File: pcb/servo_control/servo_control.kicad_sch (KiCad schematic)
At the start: 39 parts, among them J1 USB_B_Micro, J10 Conn_01x03_Female, J11 Conn_01x03_Female, J12 Conn_01x03_Female, J13 Conn_01x03_Female, J14 Conn_01x03_Female, J15 Conn_01x03_Female, J16 Conn_01x03_Female, J17 Conn_01x03_Female, J18 Conn_01x03_Female, J19 Conn_01x03_Female, J2 Conn_02x03_Counter_Clockwise, J20 Conn_01x03_Female, J3 Conn_01x03_Female, J4 Conn_01x03_Female, J5 Conn_01x03_Female, J6 Conn_01x03_Female, J7 Conn_01x03_Female, J8 Conn_01x03_Female, J9 Conn_01x03_Female, U1 ATmega2560-16A, U2 LM317_SOT-223, U3 ESP32-WROOM-32

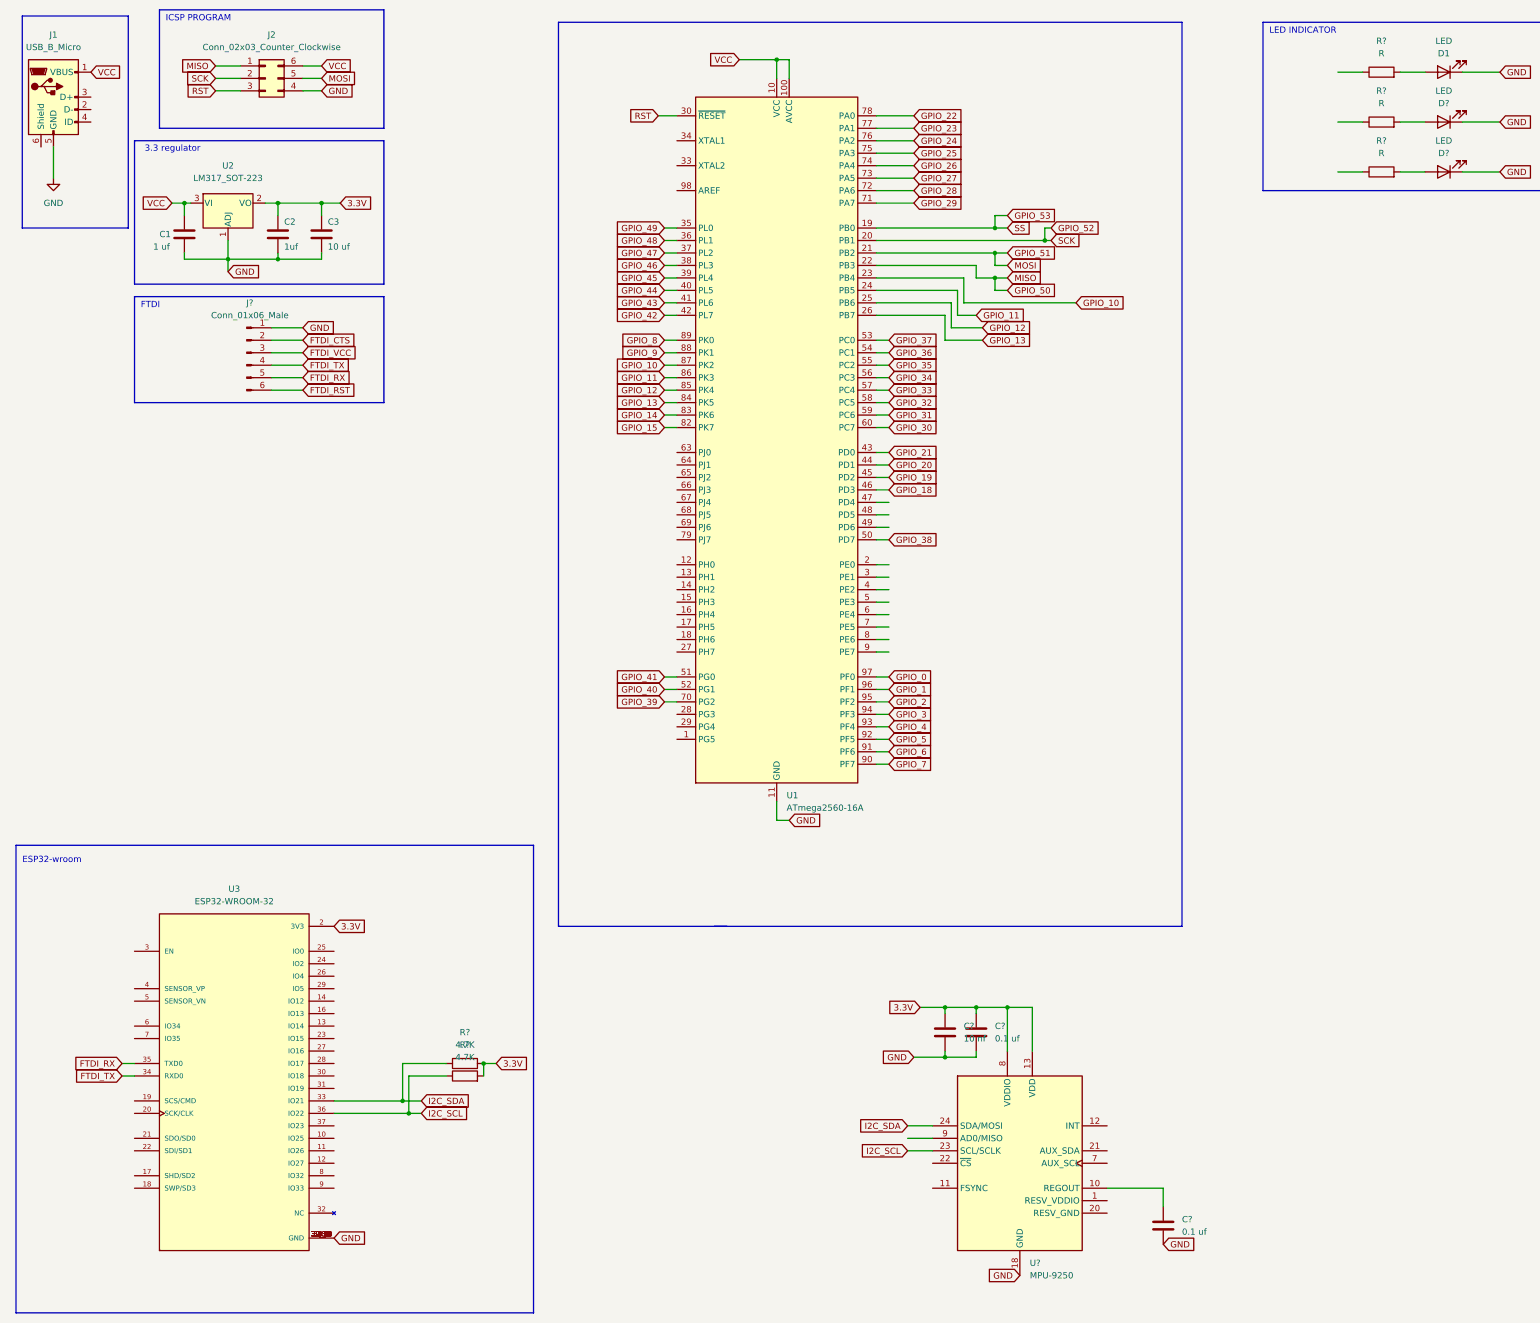
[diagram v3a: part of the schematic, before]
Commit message: add i2c
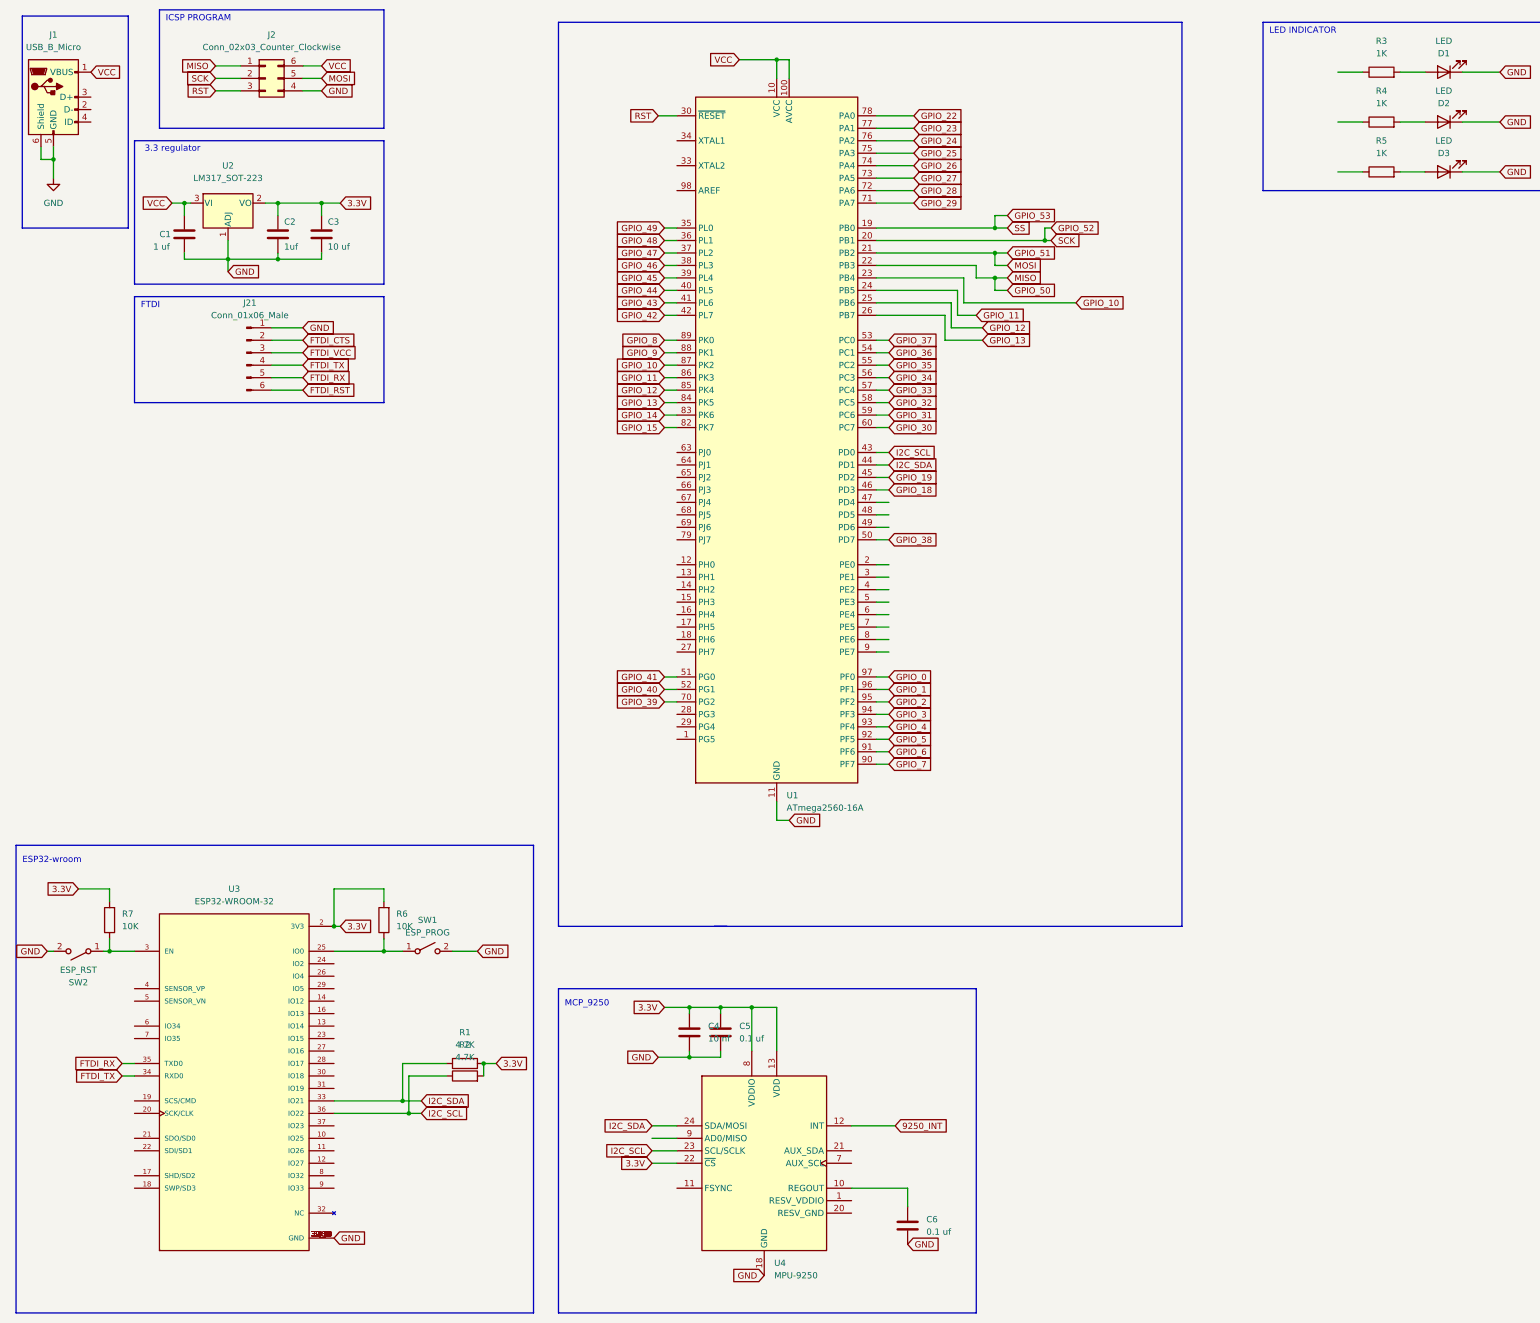
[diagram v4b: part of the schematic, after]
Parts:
- added R6, R7: 10K, Resistor_SMD:R_0603_1608Metric, symbol Device:R
- added SW1: ESP_PROG, Button_Switch_SMD:SW_DIP_SPSTx01_Slide_6.7x4.1mm_W6.73mm_P2.54mm_LowProfile_JPin, symbol Switch:SW_SPST
- added SW2: ESP_RST, Button_Switch_SMD:SW_DIP_SPSTx01_Slide_6.7x4.1mm_W6.73mm_P2.54mm_LowProfile_JPin, symbol Switch:SW_SPST
- C4, C5, C6: renamed from C?; footprint (none) -> Capacitor_SMD:C_0603_1608Metric
- J21: renamed from J?; footprint (none) -> Connector_PinHeader_2.54mm:PinHeader_1x06_P2.54mm_Vertical
- R1, R2: renamed from R?; footprint (none) -> Resistor_SMD:R_0603_1608Metric
- R3, R4, R5: renamed from R?; value R -> 1K; footprint (none) -> Resistor_SMD:R_0603_1608Metric
- gave numbers to parts that had none: 3
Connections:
- net GPIO_20 is gone; now on net I2C_SDA: U1.44 (PD1)
- net 3.3V: now also U4.22 (~{CS}), R6.2, R7.2
- net GND: now also J1.6 (Shield), SW1.2 (B), SW2.2 (B)
- net GPIO_21: no longer U1.43 (PD0)
- net I2C_SCL: now also U1.43 (PD0)
- net 9250_INT: now reaches U4.12 (INT)
- net at U3.25 (IO0): now also R6.1, SW1.1 (A)
- net at U3.3 (EN): now also R7.1, SW2.1 (A)
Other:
- note added: "MCP_9250"
- moved on the sheet: C4, C5, C6, U4

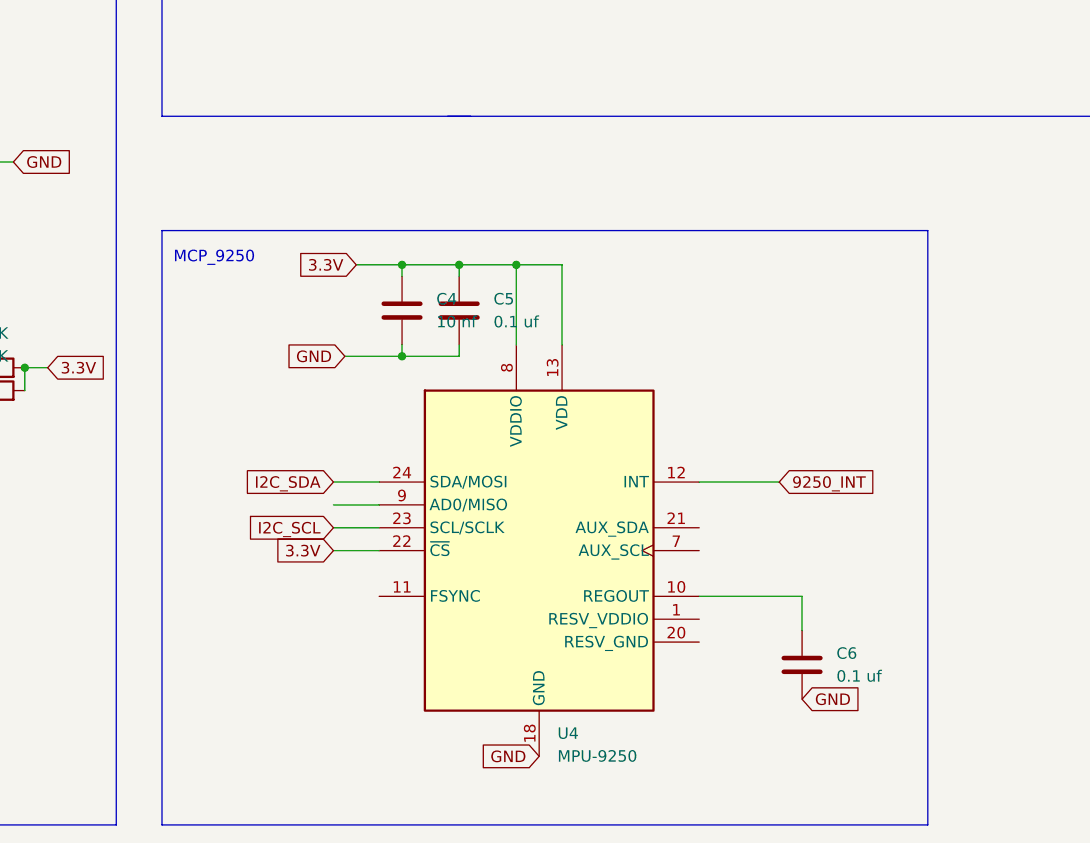
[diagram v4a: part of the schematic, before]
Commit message: add track vcc servo
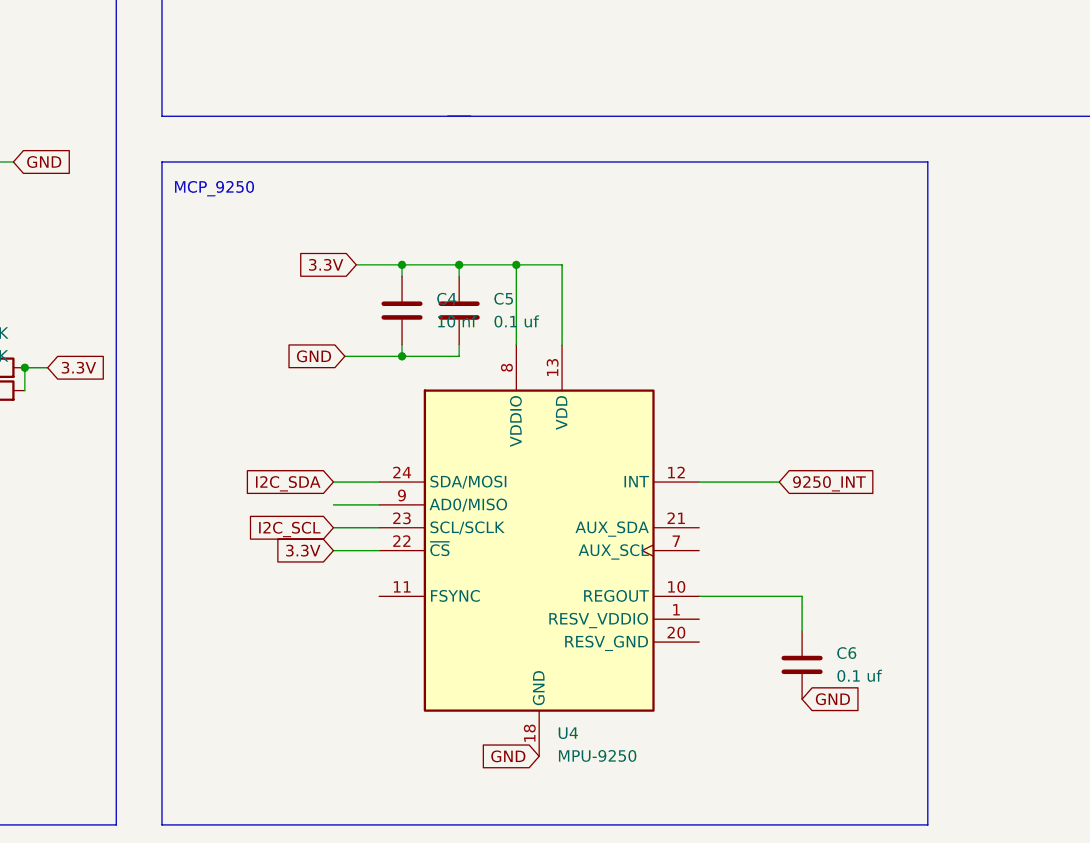
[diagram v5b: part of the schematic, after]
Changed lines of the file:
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@@
     (stroke (width 0) (type default) (color 0 0 0 0))
   )
-  (polyline (pts (xy 125.73 212.09) (xy 125.73 278.13))
+  (polyline (pts (xy 125.73 204.47) (xy 125.73 278.13))
     (stroke (width 0) (type default) (color 0 0 0 0))
   )
@@
     (stroke (width 0) (type default) (color 0 0 0 0))
   )
-  (polyline (pts (xy 125.73 212.09) (xy 210.82 212.09))
+  (polyline (pts (xy 125.73 204.47) (xy 210.82 204.47))
     (stroke (width 0) (type default) (color 0 0 0 0))
   )
@@
     (stroke (width 0) (type default) (color 0 0 0 0))
   )
-  (polyline (pts (xy 210.82 212.09) (xy 210.82 278.13))
+  (polyline (pts (xy 210.82 204.47) (xy 210.82 278.13))
     (stroke (width 0) (type default) (color 0 0 0 0))
   )
@@
     (effects (font (size 1.27 1.27)) (justify right bottom))
   )
-  (text "MCP_9250" (at 127 215.9 0)
+  (text "MCP_9250" (at 127 208.28 0)
     (effects (font (size 1.27 1.27)) (justify left bottom))
   )

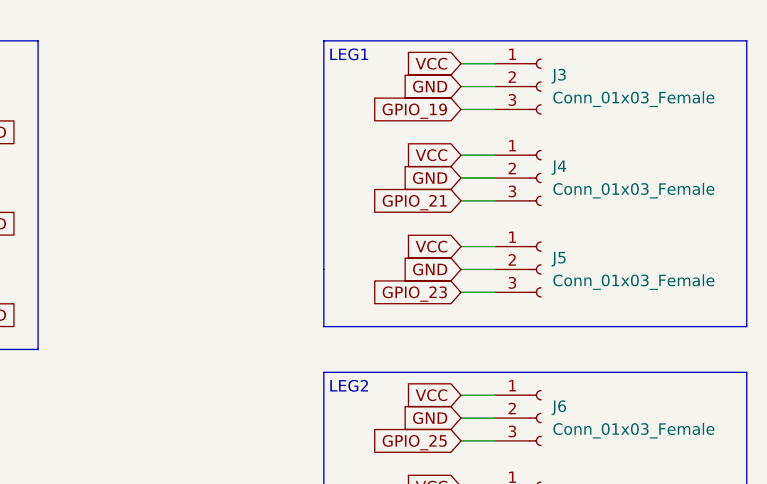
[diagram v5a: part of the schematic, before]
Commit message: add gnd zone
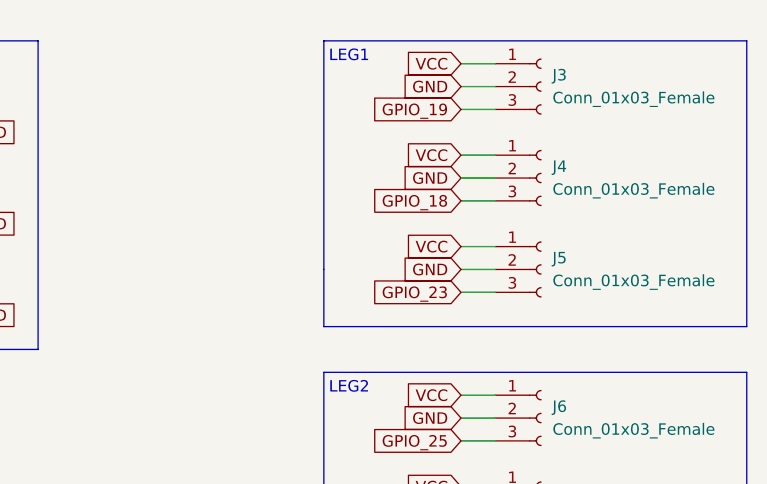
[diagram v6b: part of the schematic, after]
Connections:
- net GPIO_21 is gone; now on net GPIO_18: J4.3 (Pin_3)
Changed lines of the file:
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@@
     )
   )
-  (global_label "GPIO_21" (shape input) (at 373.38 33.02 180) (fields_autoplaced)
+  (global_label "GPIO_18" (shape input) (at 373.38 33.02 180) (fields_autoplaced)
     (effects (font (size 1.27 1.27)) (justify right))
     (property "Intersheet References" "${INTERSHEET_REFS}" (id 0) (at 363.105 32.9406 0)
